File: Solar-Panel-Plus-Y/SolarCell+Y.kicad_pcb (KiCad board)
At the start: 6 copper layers, 50 x 50 mm, 73 parts, among them J1 symbols_XF2M-1015-1A, J2 U.FL-R-SMT-1, Q1 IRLML2803, U1 TTB12G51-Balun, U2 NDS8434, U3 TSL2561, U4 Value

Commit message: More Cleanup
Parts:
- added C5: 0.1uF, Capacitor_SMD:C_0402_1005Metric, B.Cu at (181.5, 54.6)
- C1, D1, D2, R1, R2: moved to B.Cu
- D3, D4: footprint custom-footprints:MICROSMP -> misc-circuits:MICROSMP
- D5: footprint misc-circuits:SOD523 -> Diode_SMD:D_SOD-523
- J1: footprint custom-footprints:XF2M-1015-1A -> misc-circuits:XF2M-1015-1A
- J2: footprint custom-footprints:U.FL-R-SMT-1 -> misc-circuits:U.FL-R-SMT-1
- JP1: footprint custom-footprints:Burn-Wire -> SolarCellParts:Burn Wire
- SC1, SC2, SC3, SC4, SC5, SC6, SC7, SC8: footprint custom-footprints:KXOB25-05X3F -> SolarCellParts:KXOB25-05X3F
- U1: footprint custom-footprints:TTB12G51-balun -> misc-circuits:TTB12G51-balun
- U2: footprint custom-footprints:NDS8434 -> misc-circuits:NDS8434
- U3: footprint custom-footprints:TSL2561 -> misc-circuits:TSL2561
- moved D2 12.7 mm to (161.3, 79.8)
- moved D1 6.36 mm to (188.0, 53.1)
- moved C1 5.40 mm to (159.1, 58.9), turned to 90 degrees
- moved R1 4.18 mm to (158.1, 59.9), turned to 90 degrees
- moved R2 4.10 mm to (158.1, 57.9), turned to 90 degrees
- moved Ref** 2.90 mm to (152.4, 95.0)
- moved JP1 2.53 mm to (198.5, 64.9)
- moved R19 2.42 mm to (174.9, 60.5), turned to 180 degrees
- moved TP2 1.88 mm to (173.5, 72.3)
- moved D5 1.02 mm to (183.3, 54.0)
- moved R3 1.00 mm to (161.7, 49.7)
- moved R9 1.00 mm to (163.1, 49.7)
- moved TP4 0.94 mm to (183.9, 72.3)
- moved R12 0.24 mm to (172.6, 58.4)
- moved Q1 0.19 mm to (193.0, 58.8)
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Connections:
- U3 pad 5: (no net) -> unconnected-(U3-Pad5)
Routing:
- net GND: track 72.2 -> 42.7 mm, vias 14 -> 5
- net Net-(R1-Pad2): track 1.40 -> 7.09 mm, vias 0 -> 1
- net Net-(D1-Pad2): track 122.0 -> 116.9 mm, vias 0 -> 4
- net +3V3: track 56.8 -> 52.3 mm, vias 2 -> 4
- net /coil: track 13222.1 -> 13218.3 mm, vias 7 -> 6
- net Net-(D1-Pad1): track 57.9 -> 54.6 mm, vias 2 -> 5
- net VSOLAR: track 7.88 -> 5.12 mm
- net COIL_P: track 13.5 -> 14.6 mm
- net VOUT_EN: track 9.77 -> 10.4 mm
- net SCL1: track 12.9 -> 13.1 mm, vias 1 -> 2
- net SDA1: vias 1 -> 2
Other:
- board text added: "v03"
- board text removed: "v02"

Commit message: Finished Cleanup
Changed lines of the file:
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@@
   )
   (footprint "custom-footprints:ypanel" (layer "F.Cu")
-    (at 152.4 94.975 -90)
+    (at 152.4 94.974994 -90)
     (attr through_hole)
     (fp_text reference "Ref**" (at 0 0 90) (layer "F.SilkS") hide

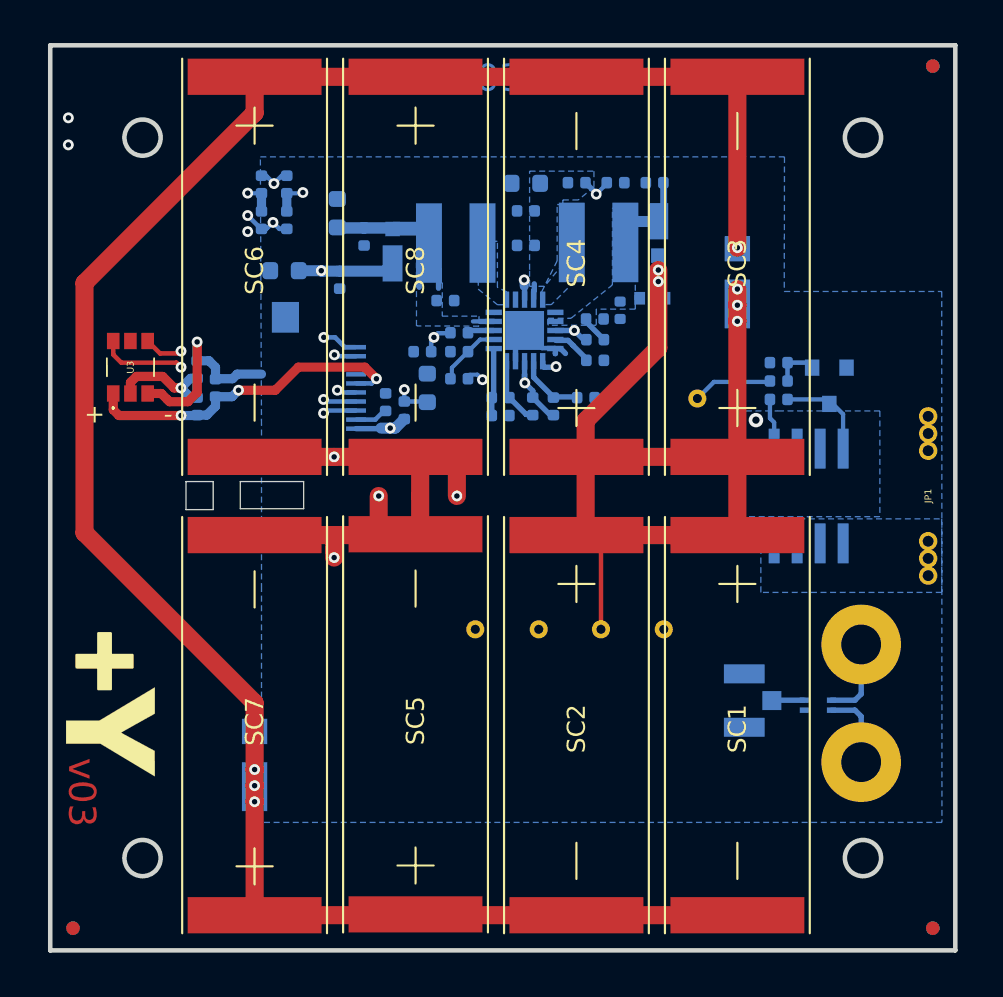
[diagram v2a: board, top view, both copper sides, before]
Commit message: Moved board connectors to North board edges
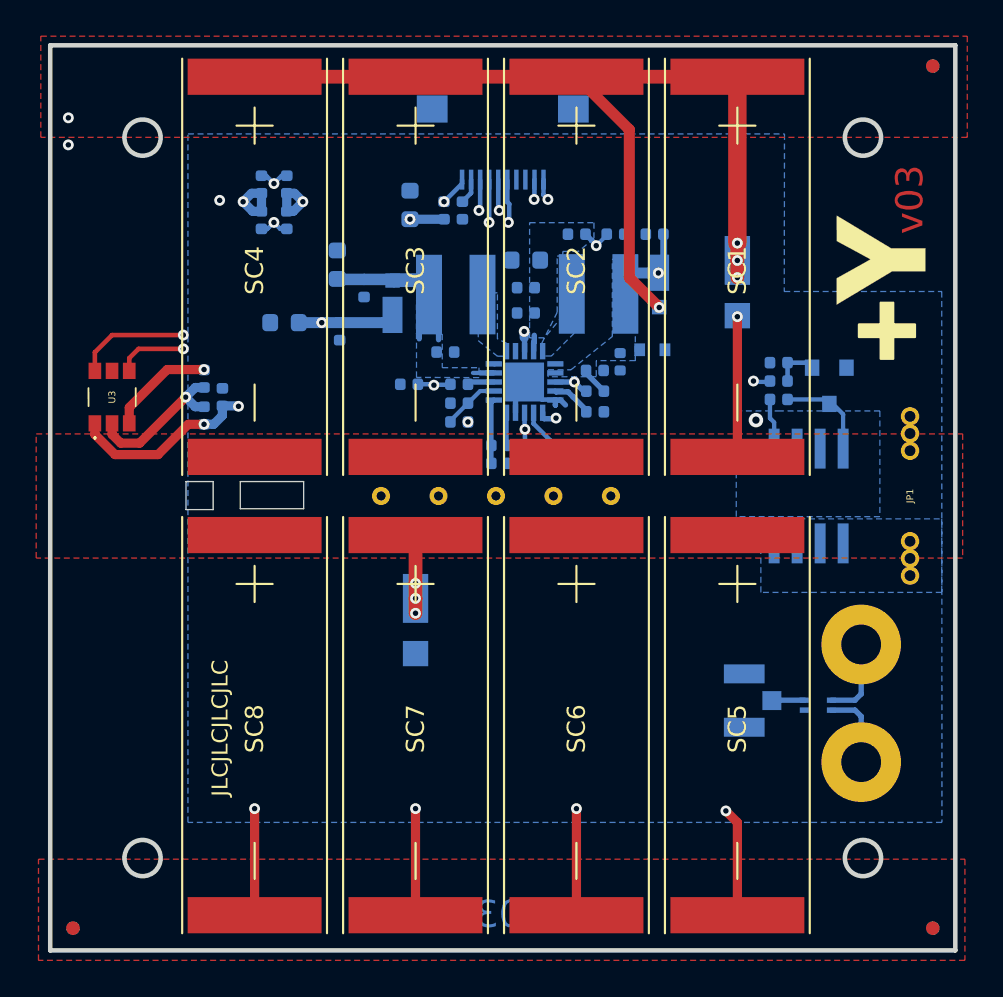
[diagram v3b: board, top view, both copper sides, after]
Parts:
- added Ref**: Val**, custom-footprints:pycubed_mini_logo, B.Cu at (166.8, 83.6)
- moved Ref** 74.8 mm to (196.8, 34.8), turned to 90 degrees
- moved SC6 30.9 mm to (179.1, 67.1)
- moved SC4 27.5 mm to (161.3, 41.7), turned to -90 degrees
- moved SC3 27.5 mm to (170.2, 41.7), turned to -90 degrees
- moved SC5 27.5 mm to (188.0, 67.1), turned to -90 degrees
- moved SC8 26.8 mm to (161.3, 67.1)
- moved SC1 25.3 mm to (188.0, 41.7)
- moved SC2 25.3 mm to (179.1, 41.7)
- moved SC7 22.8 mm to (170.2, 67.1), turned to -90 degrees
- moved J1 14.1 mm to (175.0, 47.4), turned to 0 degrees
- moved D2 12.0 mm to (170.2, 71.8), turned to -90 degrees
- moved R4 11.4 mm to (172.8, 49.1), turned to -90 degrees
- moved R25 11.3 mm to (171.8, 49.1), turned to -90 degrees
- moved C6 10.2 mm to (169.9, 48.8)
- moved TP4 9.56 mm to (177.8, 64.9)
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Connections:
- TP1 pad 1: Net-(D1-Pad1) -> VSOLAR
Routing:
- net Net-(D1-Pad2): track 116.9 -> 12.1 mm
- net /coil: track 13218.3 -> 13156.8 mm, vias 6 -> 5
- net VSOLAR: track 5.12 -> 22.6 mm, vias 0 -> 1
- net SCL1: track 13.1 -> 26.1 mm
- net SDA1: track 15.6 -> 27.2 mm
- net GND: track 42.7 -> 32.7 mm
- net COIL_P: track 14.6 -> 22.4 mm
- net BURN1: track 26.0 -> 31.3 mm, vias 1 -> 2
- net COIL_N: track 12.7 -> 17.5 mm
- net Net-(D1-Pad1): track 54.6 -> 52.4 mm, vias 5 -> 4
- net +3V3: track 52.3 -> 54.1 mm
- net Net-(R1-Pad2): track 7.09 -> 8.40 mm
- net BATT_P: track 37.8 -> 38.3 mm
- added copper zone on F.Cu, net GND
- added copper zone on F.Cu, net Net-(D1-Pad1)
- added copper zone on F.Cu, net Net-(D1-Pad2)
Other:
- board text added: "JLCJLCJLCJLC"

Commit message: Added JLC order number silkscreen
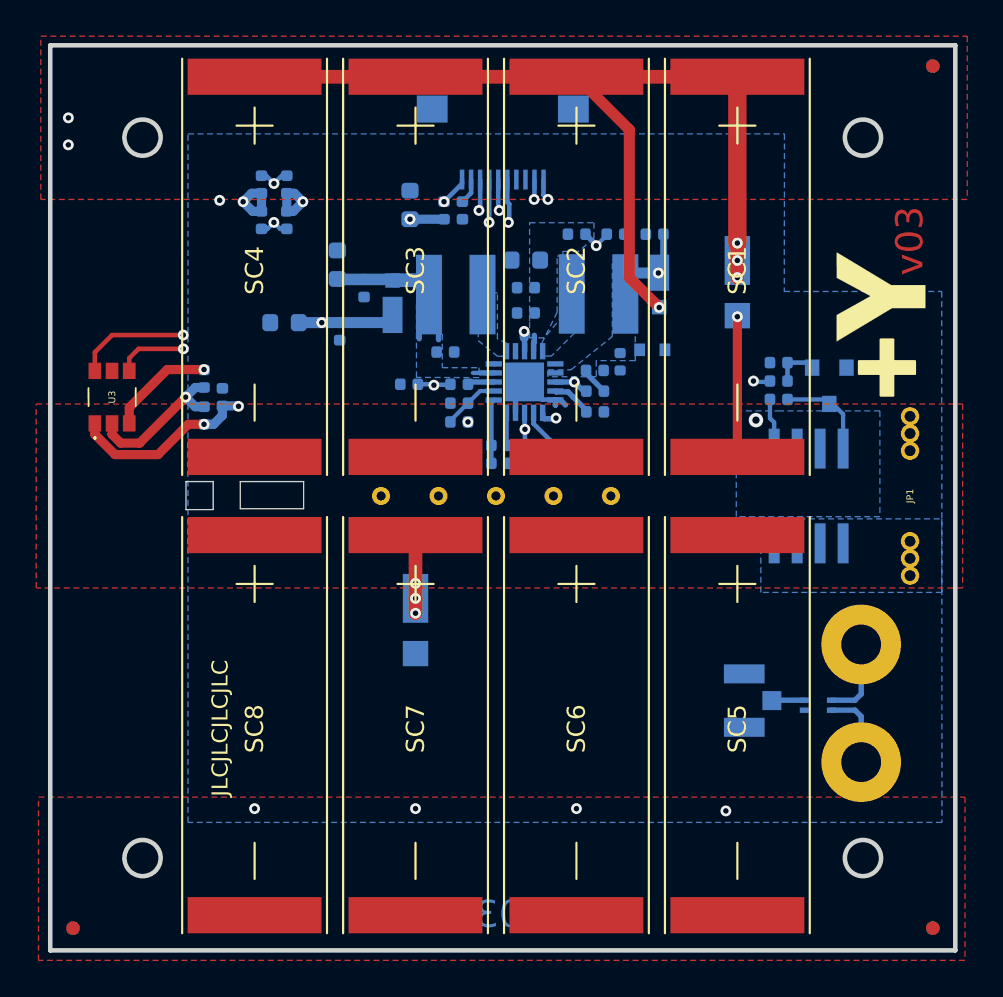
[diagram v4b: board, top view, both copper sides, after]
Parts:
- moved Ref** 2.03 mm to (196.8, 36.9)
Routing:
- net GND: track 32.7 -> 9.03 mm
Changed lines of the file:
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@@
   )
   (footprint "custom-footprints:ypanel" (layer "F.Cu")
-    (at 196.8246 34.819006 90)
+    (at 196.8246 36.851006 90)
     (attr through_hole)
     (fp_text reference "Ref**" (at 0 0 90) (layer "F.SilkS") hide
@@
   (gr_line (start 157.5 65.65) (end 159 65.65) (layer "Edge.Cuts") (width 0.05))
   (gr_line (start 164 65.6) (end 160.5 65.6) (layer "Edge.Cuts") (width 0.05))
-  (gr_text "v03" (at 197.485 48.514 90) (layer "F.Cu")
+  (gr_text "v03" (at 197.485 50.8 90) (layer "F.Cu")
     (effects (font (size 1.5 1.5) (thickness 0.3)))
   )
@@
     (effects (font (size 1.5 1.5) (thickness 0.3)))
   )
-  (gr_text "v03" (at 197.485 48.514 90) (layer "F.Mask")
+  (gr_text "v03" (at 197.485 50.8 90) (layer "F.Mask")
     (effects (font (size 1.5 1.5) (thickness 0.3)))
   )
@@
   (segment (start 161.671 49.172) (end 161.671 48.1735) (width 0.508) (layer "B.Cu") (net 3))
   (segment (start 161.671 49.172) (end 161.186 49.172) (width 0.508) (layer "B.Cu") (net 3))
-  (segment (start 179.07 88.056) (end 179.07 82.169) (width 0.508) (layer "F.Cu") (net 4))
-  (segment (start 161.29 88.056) (end 161.29 82.169) (width 0.508) (layer "F.Cu") (net 4))
   (segment (start 156.464 57.912) (end 154.366 60.01) (width 0.508) (layer "F.Cu") (net 4))
-  (segment (start 187.96 82.931) (end 187.325 82.296) (width 0.508) (layer "F.Cu") (net 4))
-  (segment (start 170.18 88.056) (end 170.18 82.169) (width 0.508) (layer "F.Cu") (net 4))
   (segment (start 158.496 57.912) (end 156.464 57.912) (width 0.508) (layer "F.Cu") (net 4))
   (segment (start 154.366 60.01) (end 154.366 60.886) (width 0.508) (layer "F.Cu") (net 4))
-  (segment (start 187.96 88.056) (end 187.96 82.931) (width 0.508) (layer "F.Cu") (net 4))
   (via (at 187.325 82.296) (size 0.6) (drill 0.3) (layers "F.Cu" "B.Cu") (net 4))
   (via (at 158.496 57.912) (size 0.6) (drill 0.3) (layers "F.Cu" "B.Cu") (net 4))
@@
         (xy 200.533 90.551)
         (xy 149.352 90.551)
-        (xy 149.352 84.963)
-        (xy 200.533 84.963)
+        (xy 149.352 81.534)
+        (xy 200.533 81.534)
       )
     )
@@
     (polygon
       (pts
-        (xy 200.406 68.326)
-        (xy 149.225 68.326)
-        (xy 149.225 61.468)
-        (xy 200.406 61.468)
+        (xy 200.406 69.977)
+        (xy 149.225 69.977)
+        (xy 149.225 59.817)
+        (xy 200.406 59.817)
       )
     )
@@
     (polygon
       (pts
-        (xy 200.66 45.085)
-        (xy 149.479 45.085)
+        (xy 200.66 48.514)
+        (xy 149.479 48.514)
         (xy 149.479 39.497)
         (xy 200.66 39.497)

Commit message: Made Requested Changes
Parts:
- removed H1, H2: MountingHole_Pad, MountingHole:MountingHole_2.2mm_M2_Pad
- removed J2: U.FL-R-SMT-1, misc-circuits:U.FL-R-SMT-1
- removed JP1: Jumper, SolarCellParts:Burn Wire
- removed Q1: IRLML2803, Package_TO_SOT_SMD:SOT-23
- removed R5, R7: 1M, Resistor_SMD:R_0402_1005Metric
- removed R6: 4.7k, Resistor_SMD:R_0402_1005Metric
- removed TP5: TP, TestPoint:TestPoint_THTPad_D1.0mm_Drill0.5mm
- removed U1: TTB12G51-Balun, misc-circuits:TTB12G51-balun
- removed U2: NDS8434, misc-circuits:NDS8434
- moved REF** 118.1 mm to (80.8, 84.2), turned to -90 degrees (x2)
- moved REF** 87.6 mm to (80.8, 36.7), turned to -90 degrees (x2)
- moved SC5 85.8 mm to (102.5, 73.8), turned to 180 degrees
- moved REF** 82.5 mm to (128.4, 84.2), turned to -90 degrees (x2)
- moved Ref** 78.6 mm to (132.7, 82.3), turned to 0 degrees
- moved SC6 76.6 mm to (102.5, 64.9), turned to 180 degrees
- moved D1 74.4 mm to (116.4, 73.4), turned to 180 degrees
- moved D2 74.2 mm to (97.8, 55.6), turned to 180 degrees
- moved TP4 73.2 mm to (104.6, 65.2), turned to -90 degrees
- moved R16 72.3 mm to (107.4, 65.1), turned to 90 degrees
- moved D5 71.6 mm to (112.7, 68.7), turned to -90 degrees
- moved C4 71.0 mm to (109.3, 65.5), turned to -90 degrees
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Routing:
- net /coil: track 13156.8 -> 12938.3 mm
- net BURN1: track 31.3 -> 0.00 mm, vias 2 -> 0
- net BATT_P: track 38.3 -> 22.1 mm, vias 2 -> 1
- net SDA1: track 27.2 -> 40.8 mm
- net SCL1: track 26.1 -> 38.3 mm
- net /VBAT: track 13.7 -> 24.8 mm
- net COIL_P: track 22.4 -> 13.4 mm
- net Net-(Q1-Pad3): track 5.31 -> 0.00 mm
- net Net-(H2-Pad1): track 4.52 -> 0.00 mm
- net Net-(H1-Pad1): track 4.32 -> 0.00 mm
- net COIL_N: track 17.5 -> 13.3 mm
- net Net-(Q1-Pad1): track 2.49 -> 0.00 mm
- net VSOLAR: track 22.6 -> 20.4 mm
- net GND: track 9.03 -> 7.13 mm
- net Net-(J2-Pad3): track 1.80 -> 0.00 mm
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- removed copper zone on B.Cu, net /VBURN
- removed copper zone on B.Cu, net BATT_P
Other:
- outline, holes or cut-outs redrawn
- rule pad_to_mask_clearance: 0.049 -> 0.0508
- board text removed: "BURN"
